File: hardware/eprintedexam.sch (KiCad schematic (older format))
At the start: 54 parts, among them J1 Conn_01x04, J2 Conn_01x08, Q1 2N7002, Q2 2N7002, Q3 2N7002, Q4 2N7002, Q5 2N7002, Q6 2N7002, Q7 2N7002, Q8 2N7002, SW1 SW_Push, SW2 SW_Push, SW3 SW_Push, SW4 SW_Push, U1 AP1117-33, U2 ESP-12F

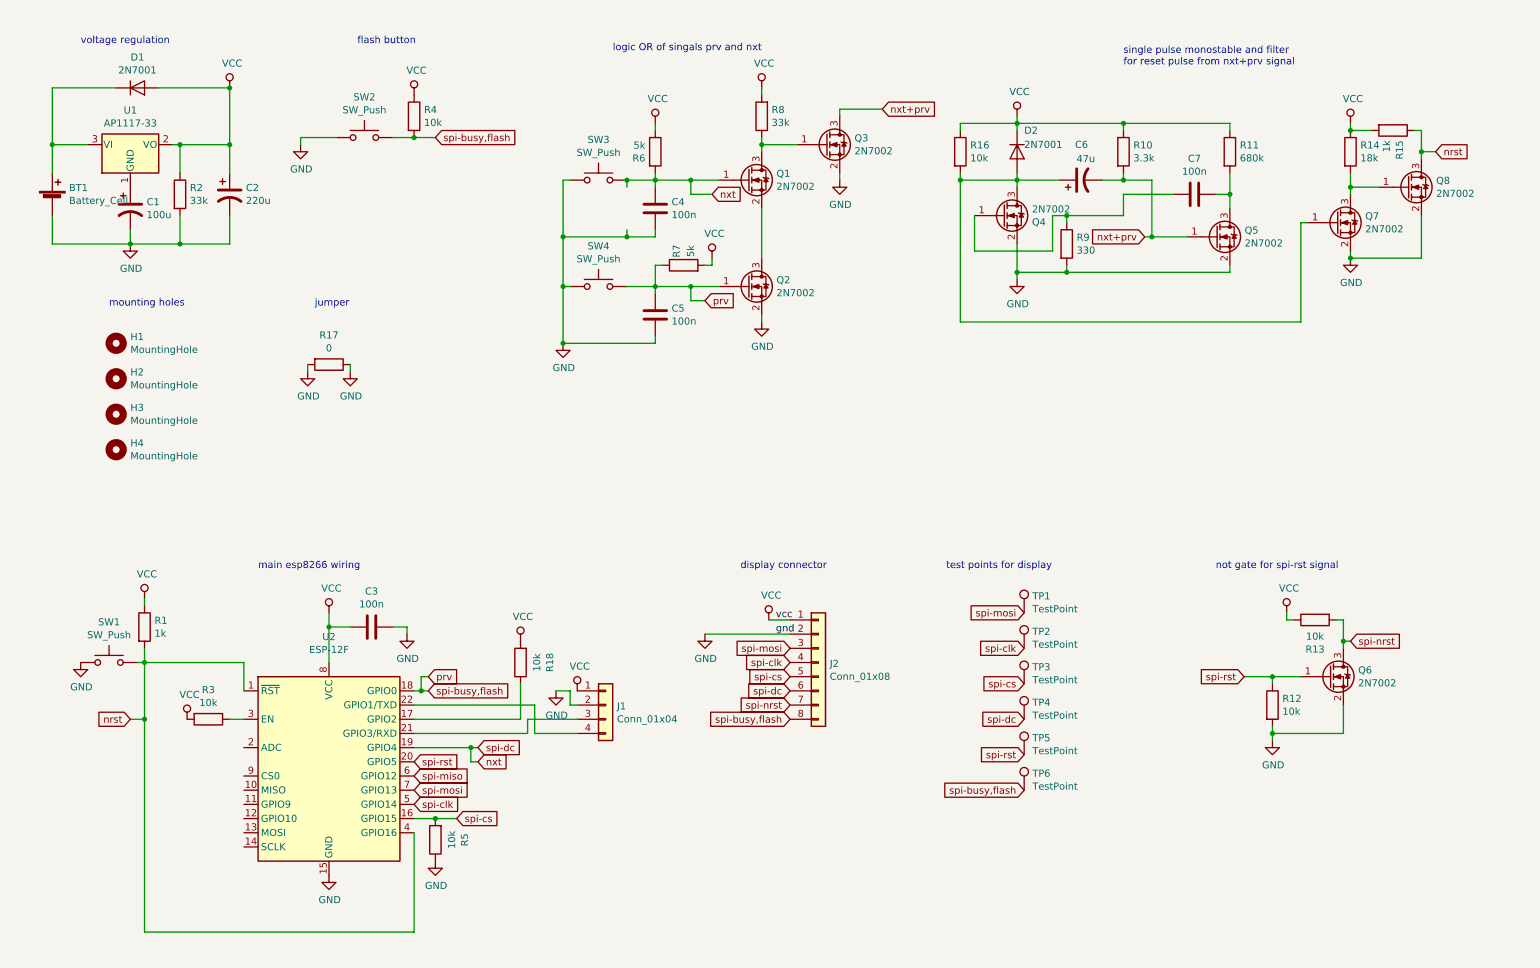
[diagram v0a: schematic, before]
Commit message: redesing pcb and added isolation mosfets
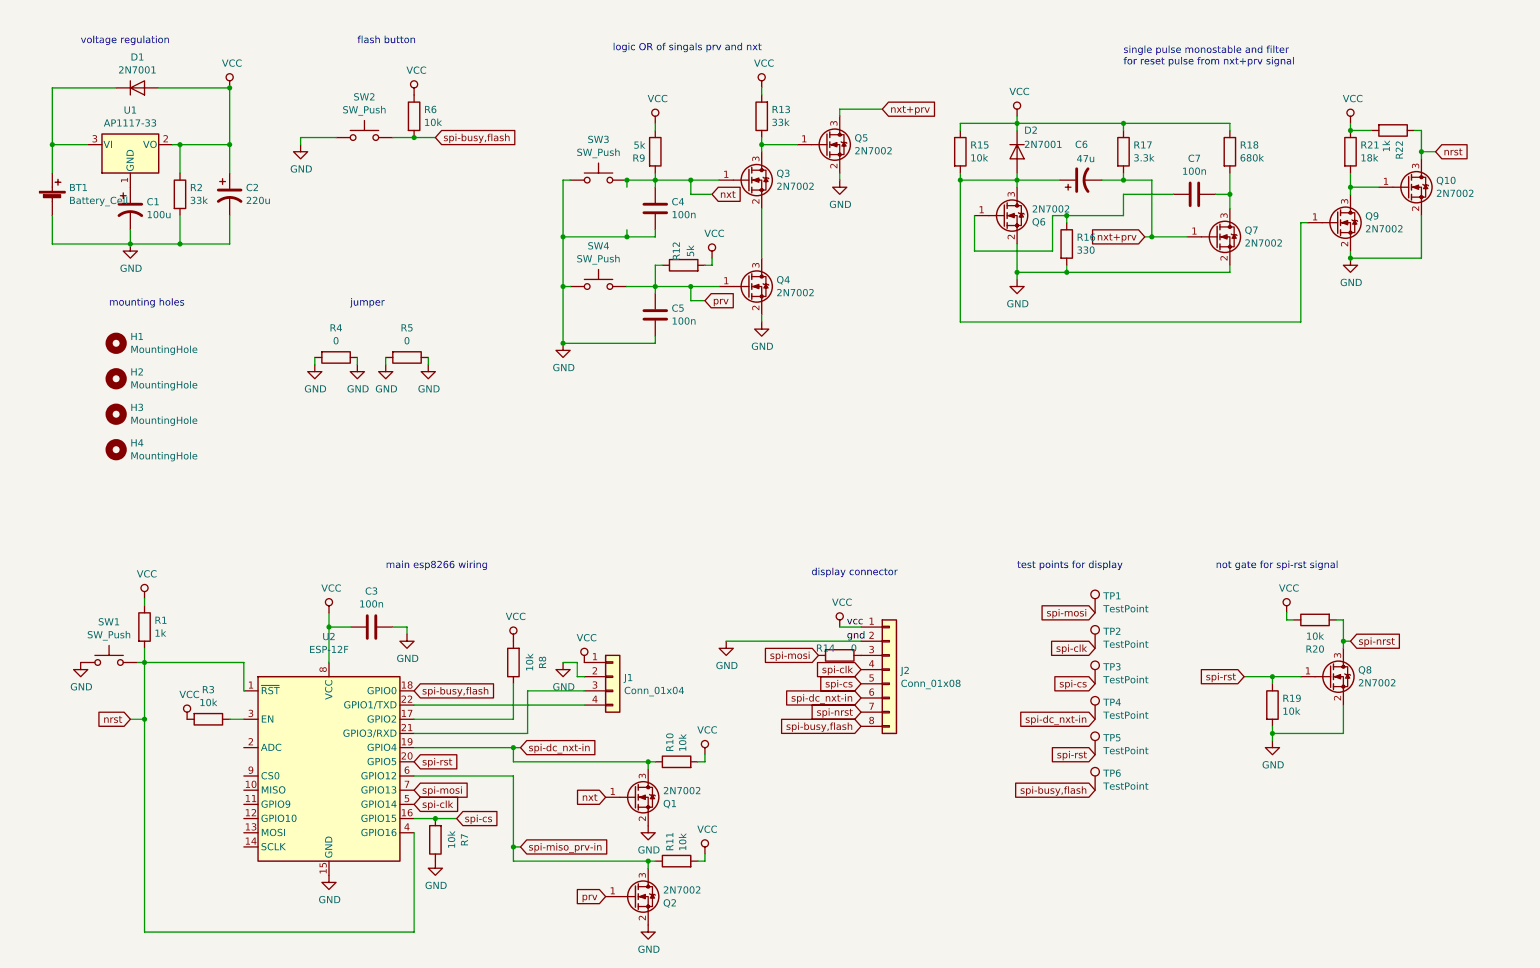
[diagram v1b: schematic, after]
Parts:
- added Q1, Q2: 2N7002, Package_TO_SOT_SMD:SOT-23, symbol Transistor_FET:2N7002
- added R10, R11: 10k, Resistor_SMD:R_1206_3216Metric, symbol Device:R
- added R14, R5: 0, Resistor_SMD:R_1206_3216Metric, symbol Device:R
- R15: renamed from R16; footprint Resistor_THT:R_Axial_DIN0207_L6.3mm_D2.5mm_P10.16mm_Horizontal -> Resistor_SMD:R_1206_3216Metric
- renumbered Q8 to Q10, Q1 to Q3, Q2 to Q4, Q3 to Q5, Q4 to Q6, Q5 to Q7, Q6 to Q8, Q7 to Q9, R7 to R12, R8 to R13, R9 to R16, R10 to R17, R11 to R18, R12 to R19, R13 to R20, R14 to R21, R15 to R22, R17 to R4, R4 to R6, R5 to R7, R18 to R8, R6 to R9
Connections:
- net GND: now also Q1.2 (S), Q2.2 (S), R5.1, R5.2
- net VCC: now also R10.2, R11.2
- net nxt: now also Q1.1 (G); no longer J2.6 (Pin_6), TP4.1, U2.19 (GPIO4)
- net prv: now also Q2.1 (G); no longer J2.8 (Pin_8), R6.2, SW2.2, TP6.1, U2.18 (GPIO0)
- net spi-mosi: now also R14.2; no longer J2.3 (Pin_3)
- net spi-miso renamed spi-miso_prv-in
- net spi-miso_prv-in: now also Q2.3 (D), R11.1
- new net: J2.3 (Pin_3), R14.1
- new net spi-busy,flash: J2.8 (Pin_8), R6.2, SW2.2, TP6.1, U2.18 (GPIO0)
- new net spi-dc_nxt-in: J2.6 (Pin_6), Q1.3 (D), R10.1, TP4.1, U2.19 (GPIO4)
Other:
- moved on the sheet: J1, J2, R4, R8, TP1, TP2, TP3, TP4, TP5, TP6

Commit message: the hardware works
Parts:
- removed Q8: 2N7002, Package_TO_SOT_SMD:SOT-23, symbol Transistor_FET:2N7002
- removed R1: 1k, Resistor_SMD:R_1206_3216Metric, symbol Device:R
- removed R19, R20: 10k, Resistor_SMD:R_1206_3216Metric, symbol Device:R
- removed R4: 0, Resistor_SMD:R_1206_3216Metric, symbol Device:R
- R20: renamed from R22; value 1k -> 10k
- renumbered Q9 to Q8, Q10 to Q9, R21 to R19, R5 to R4
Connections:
- net spi-nrst is gone; now on net spi-rst: J2.7 (Pin_7)
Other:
- note removed: "not gate for spi-rst signal"
- moved on the sheet: BT1, C1, C2, C3, C4, C5, C6, C7, D1, D2, H1, H2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

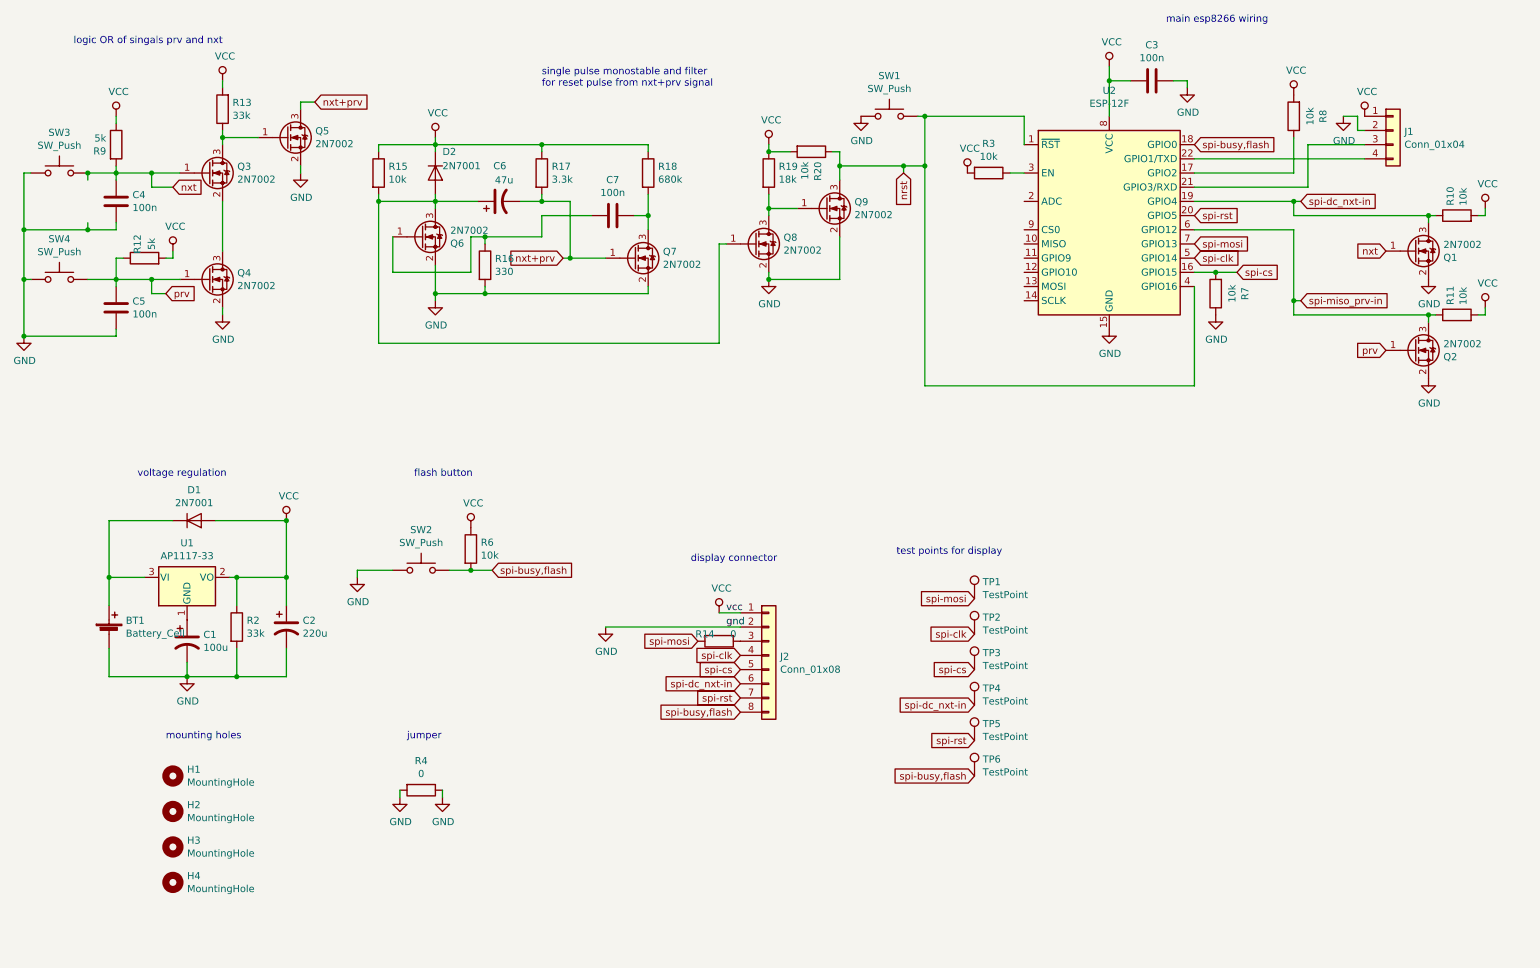
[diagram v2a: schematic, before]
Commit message: decoupled esp to monostable via button trace
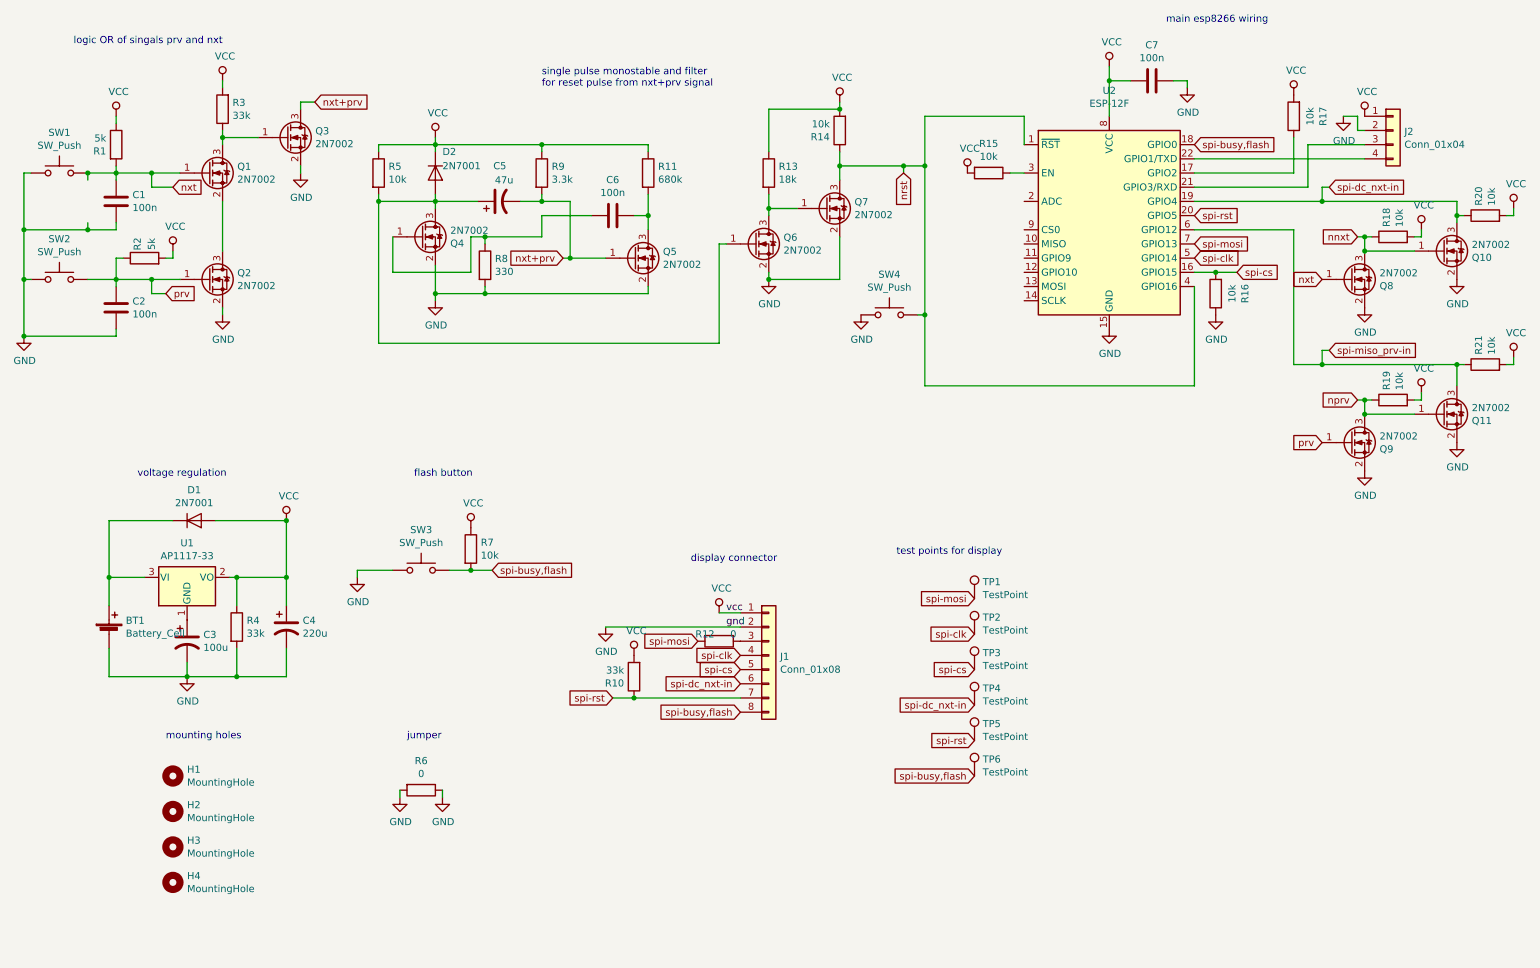
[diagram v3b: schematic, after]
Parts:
- added Q8, Q9: 2N7002, Package_TO_SOT_SMD:SOT-23, symbol Transistor_FET:2N7002
- added R10: 33k, Resistor_SMD:R_1206_3216Metric, symbol Device:R
- added R18, R19: 10k, Resistor_SMD:R_1206_3216Metric, symbol Device:R
- C3: renamed from C1; footprint Capacitor_THT:CP_Radial_D8.0mm_P5.00mm -> Capacitor_THT:CP_Radial_D6.3mm_P2.50mm
- C4: renamed from C2; footprint Capacitor_THT:CP_Radial_D10.0mm_P5.00mm -> Capacitor_THT:CP_Radial_D6.3mm_P2.50mm
- renumbered C4 to C1, C5 to C2, C6 to C5, C7 to C6, C3 to C7, J2 to J1, J1 to J2, Q3 to Q1, Q1 to Q10, Q2 to Q11, Q4 to Q2, Q5 to Q3, Q6 to Q4, Q7 to Q5, Q8 to Q6, Q9 to Q7, R9 to R1, R18 to R11, R14 to R12, R19 to R13, R20 to R14, R3 to R15, R7 to R16, R8 to R17, R12 to R2, R10 to R20, R11 to R21, R13 to R3, R2 to R4, R15 to R5, R4 to R6, R6 to R7, R16 to R8, R17 to R9, SW3 to SW1, SW4 to SW2, SW2 to SW3, SW1 to SW4
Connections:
- net GND: now also Q8.2 (S), Q9.2 (S)
- net VCC: now also R10.2, R18.2, R19.2
- net nxt: now also Q8.1 (G); no longer Q10.1 (G)
- net prv: now also Q9.1 (G); no longer Q11.1 (G)
- net spi-rst: now also R10.1
- new net nnxt: Q10.1 (G), Q8.3 (D), R18.1
- new net nprv: Q11.1 (G), Q9.3 (D), R19.1
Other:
- moved on the sheet: Q10, Q11, R14, R20, R21, SW4

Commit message: final update
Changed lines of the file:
@@
 	1    0    0    -1
 $EndComp
-Wire Wire Line
-	1100 2100 650  2100
-Wire Wire Line
-	1300 2100 1100 2100
-Connection ~ 1100 2100
-Wire Wire Line
-	1100 2050 1100 2100
-Connection ~ 1100 1700
-Wire Wire Line
-	1100 1700 1100 1750
 $Comp
 L Transistor_FET:2N7002 Q8
@@
 	1    0    0    -1
 $EndComp
+Wire Wire Line
+	650  2100 1300 2100
 $EndSCHEMATC
